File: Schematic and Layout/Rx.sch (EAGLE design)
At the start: 21 parts

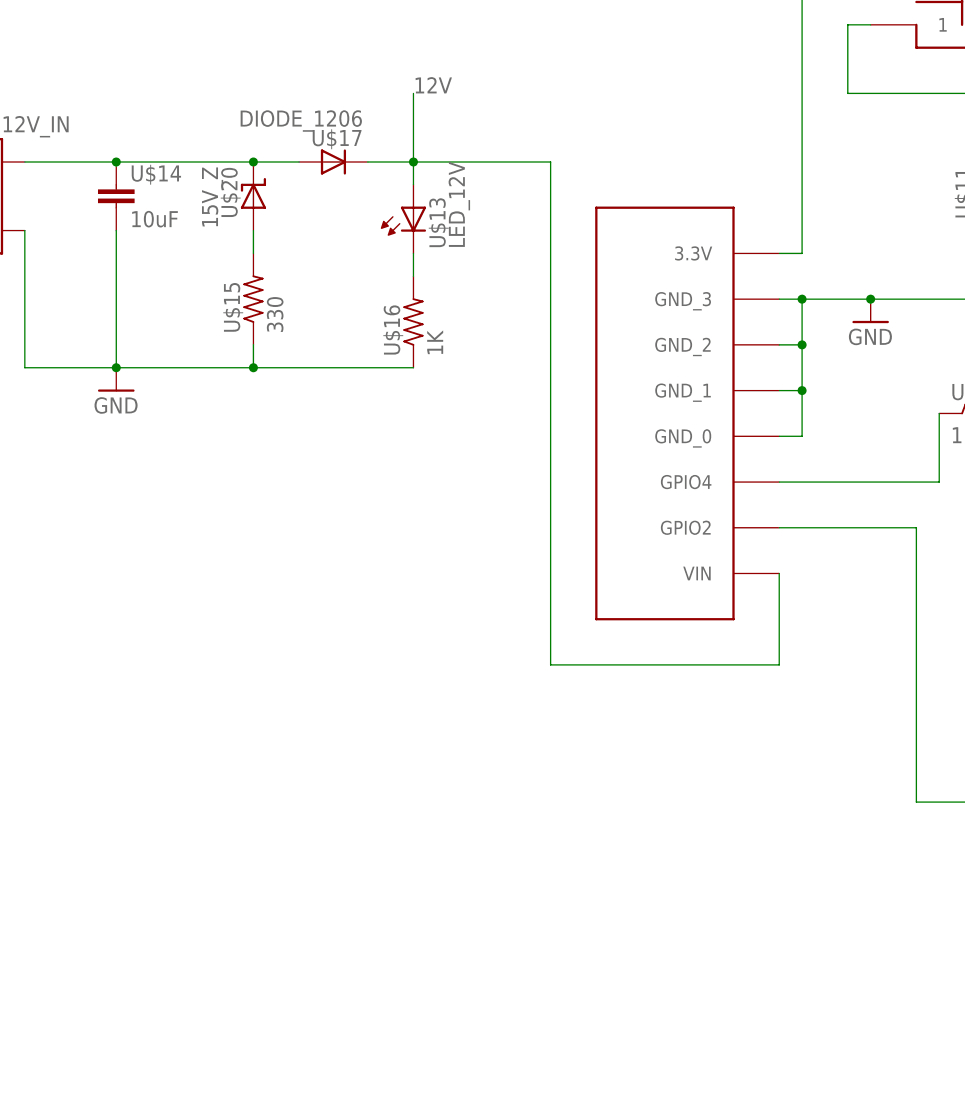
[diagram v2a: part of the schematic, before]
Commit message: ESPs now run off of 5 V
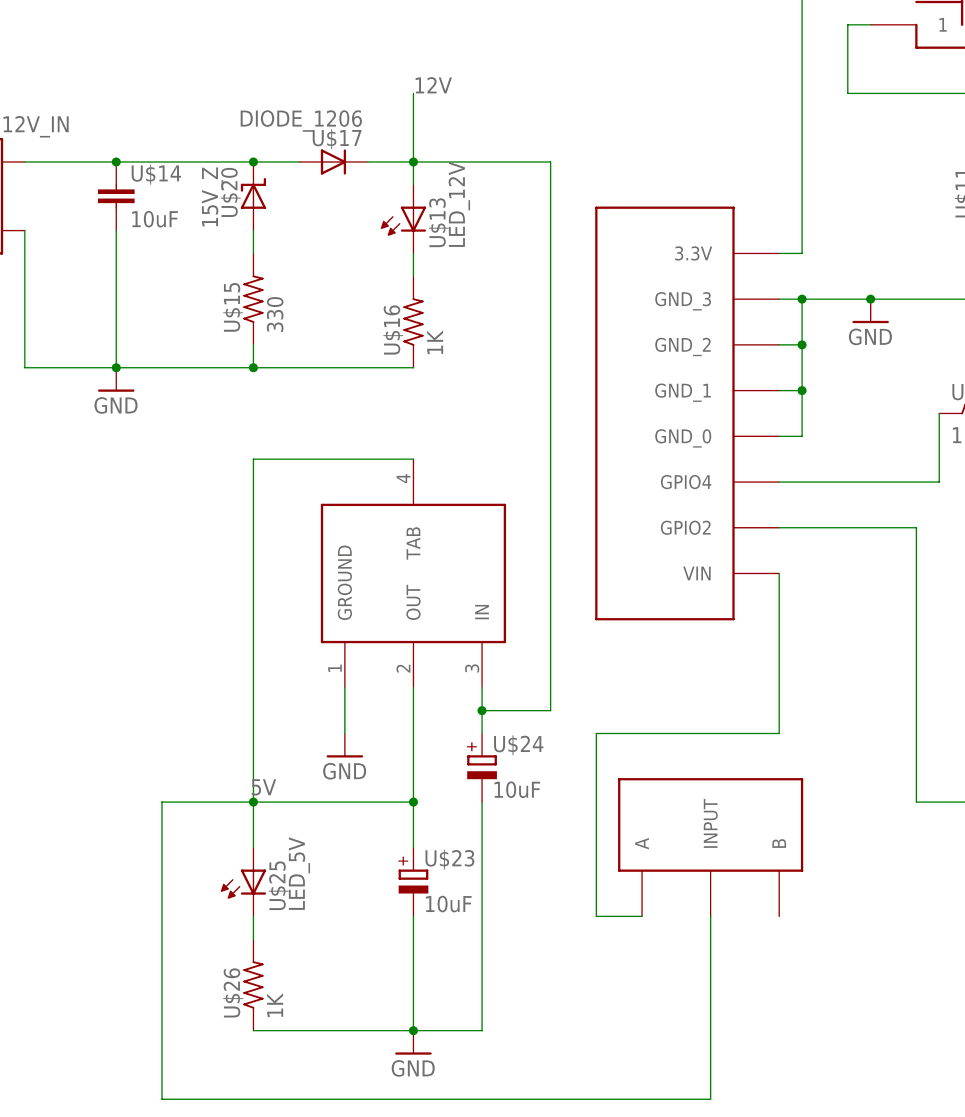
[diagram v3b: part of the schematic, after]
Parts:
- added U$22: 5V_REG, Gas_Sensor_Lib_v1:5V_REG
- added U$23, U$24: 10uF, Gas_Sensor_Lib_v1:CAP_POL
- added U$25: LED_5V, Gas_Sensor_Lib_v1:LED_1206
- added U$26: 1K, Gas_Sensor_Lib_v1:RES
- added U$27: SPDT, Gas_Sensor_Lib_v1:SPDT
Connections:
- new net 5V: U$22.OUT, U$22.TAB, U$23.+, U$25.HI, U$27.INPUT
- new net N$13: U$27.A, U$9.VIN
- new net N$8: U$25.LO, U$26.2
- net 12V: now also U$22.IN, U$24.+; no longer U$9.VIN
- net GND: now also U$22.GROUND, U$23.-, U$24.-, U$26.1
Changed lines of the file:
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@@
 <part name="U$21" library="Gas_Sensor_Lib_v1" deviceset="RES" device="" value="1K"/>
 <part name="GND5" library="supply1" deviceset="GND" device=""/>
+<part name="U$22" library="Gas_Sensor_Lib_v1" deviceset="5V_REG" device=""/>
+<part name="U$23" library="Gas_Sensor_Lib_v1" deviceset="CAP_POL" device="" value="10uF"/>
+<part name="U$24" library="Gas_Sensor_Lib_v1" deviceset="CAP_POL" device="" value="10uF"/>
+<part name="GND6" library="supply1" deviceset="GND" device=""/>
+<part name="GND7" library="supply1" deviceset="GND" device=""/>
+<part name="U$25" library="Gas_Sensor_Lib_v1" deviceset="LED_1206" device="" value="LED_5V"/>
+<part name="U$26" library="Gas_Sensor_Lib_v1" deviceset="RES" device="" value="1K"/>
+<part name="U$27" library="Gas_Sensor_Lib_v1" deviceset="SPDT" device=""/>
 </parts>
 <sheets>
@@
 <instance part="U$21" gate="G$1" x="63.5" y="7.62" rot="R90"/>
 <instance part="GND5" gate="1" x="63.5" y="-2.54"/>
+<instance part="U$22" gate="G$1" x="-25.4" y="12.7"/>
+<instance part="U$23" gate="G$1" x="-25.4" y="-17.78"/>
+<instance part="U$24" gate="G$1" x="-17.78" y="-5.08"/>
+<instance part="GND6" gate="1" x="-25.4" y="-38.1"/>
+<instance part="GND7" gate="1" x="-33.02" y="-5.08"/>
+<instance part="U$25" gate="G$1" x="-43.18" y="-17.78"/>
+<instance part="U$26" gate="G$1" x="-43.18" y="-30.48" rot="R90"/>
+<instance part="U$27" gate="G$1" x="7.62" y="-15.24"/>
 </instances>
 <busses>
@@
 <wire x1="63.5" y1="2.54" x2="63.5" y2="0" width="0.1524" layer="91"/>
 </segment>
+<segment>
+<pinref part="GND6" gate="1" pin="GND"/>
+<pinref part="U$23" gate="G$1" pin="-"/>
+<wire x1="-25.4" y1="-22.86" x2="-25.4" y2="-35.56" width="0.1524" layer="91"/>
+<pinref part="U$26" gate="G$1" pin="1"/>
+<wire x1="-43.18" y1="-35.56" x2="-25.4" y2="-35.56" width="0.1524" layer="91"/>
+<junction x="-25.4" y="-35.56"/>
+<pinref part="U$24" gate="G$1" pin="-"/>
+<wire x1="-17.78" y1="-10.16" x2="-17.78" y2="-35.56" width="0.1524" layer="91"/>
+<wire x1="-17.78" y1="-35.56" x2="-25.4" y2="-35.56" width="0.1524" layer="91"/>
+</segment>
+<segment>
+<pinref part="U$22" gate="G$1" pin="GROUND"/>
+<pinref part="GND7" gate="1" pin="GND"/>
+<wire x1="-33.02" y1="2.54" x2="-33.02" y2="-2.54" width="0.1524" layer="91"/>
+</segment>
 </net>
 <net name="N$3" class="0">
@@
 <wire x1="-25.4" y1="60.96" x2="-25.4" y2="68.58" width="0.1524" layer="91"/>
 <label x="-25.4" y="68.58" size="1.778" layer="95"/>
-<pinref part="U$9" gate="G$1" pin="VIN"/>
-<wire x1="15.24" y1="15.24" x2="15.24" y2="5.08" width="0.1524" layer="91"/>
-<wire x1="15.24" y1="5.08" x2="-10.16" y2="5.08" width="0.1524" layer="91"/>
-<wire x1="-10.16" y1="5.08" x2="-10.16" y2="60.96" width="0.1524" layer="91"/>
+<wire x1="-10.16" y1="0" x2="-10.16" y2="60.96" width="0.1524" layer="91"/>
 <wire x1="-25.4" y1="60.96" x2="-10.16" y2="60.96" width="0.1524" layer="91"/>
+<pinref part="U$24" gate="G$1" pin="+"/>
+<pinref part="U$22" gate="G$1" pin="IN"/>
+<wire x1="-17.78" y1="2.54" x2="-17.78" y2="0" width="0.1524" layer="91"/>
+<wire x1="-17.78" y1="0" x2="-17.78" y2="-2.54" width="0.1524" layer="91"/>
+<wire x1="-10.16" y1="0" x2="-17.78" y2="0" width="0.1524" layer="91"/>
+<junction x="-17.78" y="0"/>
 </segment>
 <segment>
@@
 </segment>
 </net>
+<net name="5V" class="0">
+<segment>
+<pinref part="U$22" gate="G$1" pin="OUT"/>
+<pinref part="U$23" gate="G$1" pin="+"/>
+<wire x1="-25.4" y1="2.54" x2="-25.4" y2="-10.16" width="0.1524" layer="91"/>
+<label x="-40.64" y="-7.62" size="1.778" layer="95" rot="R180"/>
+<pinref part="U$22" gate="G$1" pin="TAB"/>
+<wire x1="-25.4" y1="-10.16" x2="-25.4" y2="-15.24" width="0.1524" layer="91"/>
+<wire x1="-25.4" y1="27.94" x2="-43.18" y2="27.94" width="0.1524" layer="91"/>
+<wire x1="-43.18" y1="27.94" x2="-43.18" y2="-10.16" width="0.1524" layer="91"/>
+<wire x1="-43.18" y1="-10.16" x2="-25.4" y2="-10.16" width="0.1524" layer="91"/>
+<junction x="-25.4" y="-10.16"/>
+<pinref part="U$25" gate="G$1" pin="HI"/>
+<wire x1="-43.18" y1="-10.16" x2="-43.18" y2="-15.24" width="0.1524" layer="91"/>
+<junction x="-43.18" y="-10.16"/>
+<wire x1="-43.18" y1="-10.16" x2="-53.34" y2="-10.16" width="0.1524" layer="91"/>
+<wire x1="-53.34" y1="-10.16" x2="-53.34" y2="-43.18" width="0.1524" layer="91"/>
+<wire x1="-53.34" y1="-43.18" x2="7.62" y2="-43.18" width="0.1524" layer="91"/>
+<pinref part="U$27" gate="G$1" pin="INPUT"/>
+<wire x1="7.62" y1="-43.18" x2="7.62" y2="-22.86" width="0.1524" layer="91"/>
+</segment>
+</net>
+<net name="N$8" class="0">
+<segment>
+<pinref part="U$25" gate="G$1" pin="LO"/>
+<pinref part="U$26" gate="G$1" pin="2"/>
+<wire x1="-43.18" y1="-22.86" x2="-43.18" y2="-25.4" width="0.1524" layer="91"/>
+</segment>
+</net>
+<net name="N$13" class="0">
+<segment>
+<pinref part="U$27" gate="G$1" pin="A"/>
+<wire x1="0" y1="-22.86" x2="-5.08" y2="-22.86" width="0.1524" layer="91"/>
+<wire x1="-5.08" y1="-22.86" x2="-5.08" y2="-2.54" width="0.1524" layer="91"/>
+<pinref part="U$9" gate="G$1" pin="VIN"/>
+<wire x1="-5.08" y1="-2.54" x2="15.24" y2="-2.54" width="0.1524" layer="91"/>
+<wire x1="15.24" y1="-2.54" x2="15.24" y2="15.24" width="0.1524" layer="91"/>
+</segment>
+</net>
